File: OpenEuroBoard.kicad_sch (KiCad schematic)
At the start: 143 parts, among them J1 Eurorack_bus_mini, J10 Jack 4, J11 Conn_01x08, J12 Jack 5, J13 Jack 6, J14 Jack 7, J15 Jack 8, J16 Conn_01x04, J17 MIDI_in, J18 Conn_01x03, J19 Conn_01x03, J2 Conn_01x07, J20 Conn_01x03, J21 MIDI_out, J22 Conn_01x03, J23 Conn_01x05, J24 Conn_01x03, J25 Conn_01x05, J26 Conn_01x03, J27 Conn_01x08, J28 Conn_01x08, J29 Conn_01x04, J3 Conn_01x07, J30 Screw_Terminal_01x01, J31 Conn_01x05, J32 Conn_01x03, J33 Conn_01x05, J34 Conn_01x03, J35 Conn_01x05, J36 Conn_01x03, J37 Screw_Terminal_01x01, J38 Screw_Terminal_01x01, J39 Conn_01x05, J4 Conn_01x07, J40 Conn_01x03, J41 Conn_01x03, J42 Conn_01x05, J43 Conn_01x03, J44 Conn_01x03, J45 Conn_01x02, J46 Conn_01x04, J47 Screw_Terminal_01x01, J48 Screw_Terminal_01x01, J49 Screw_Terminal_01x01, J5 Conn_01x07, J50 Screw_Terminal_01x01, J51 Screw_Terminal_01x01, J52 Conn_01x04, J53 Conn_01x04, J54 Conn_01x04, J55 Jumpers, J56 Conn_01x04, J57 Conn_01x08, J58 Conn_01x02, J59 AudioJack3_Ground, J6 Jack 1, J7 Jack 2, J8 Conn_01x08, J9 Jack 3, SW1 SW_Push, SW10 SW_SPDT, SW11 SW_SPDT, SW12 SW_SPDT, SW2 SW_Push, SW3 SW_Push, SW4 SW_Push, SW5 SW_Push, SW6 SW_Push, SW7 SW_SPDT, SW8 SW_SPDT, SW9 SW_SPDT, U1 LM1117IMP-5, U2 TL074, U3 TL074, U4 CD40107BE, U5 6N139, U6 TL074, U7 TL072, U8 TL074

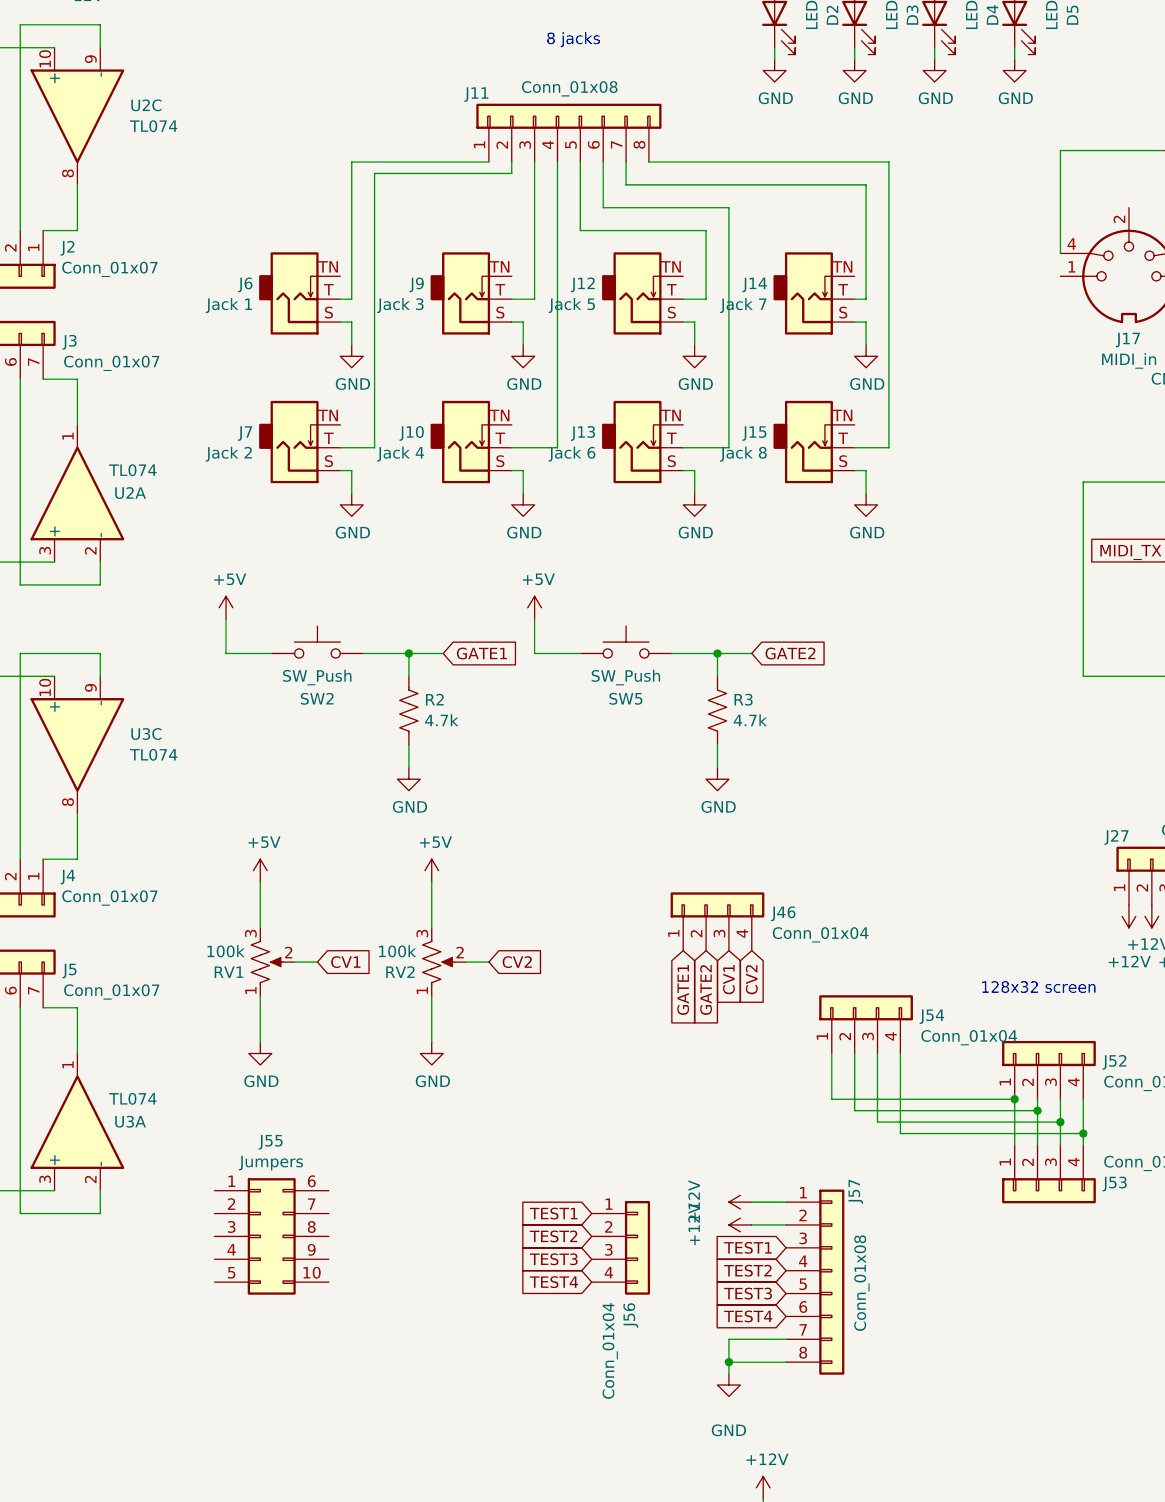
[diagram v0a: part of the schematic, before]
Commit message: Add connector for normals to jacks
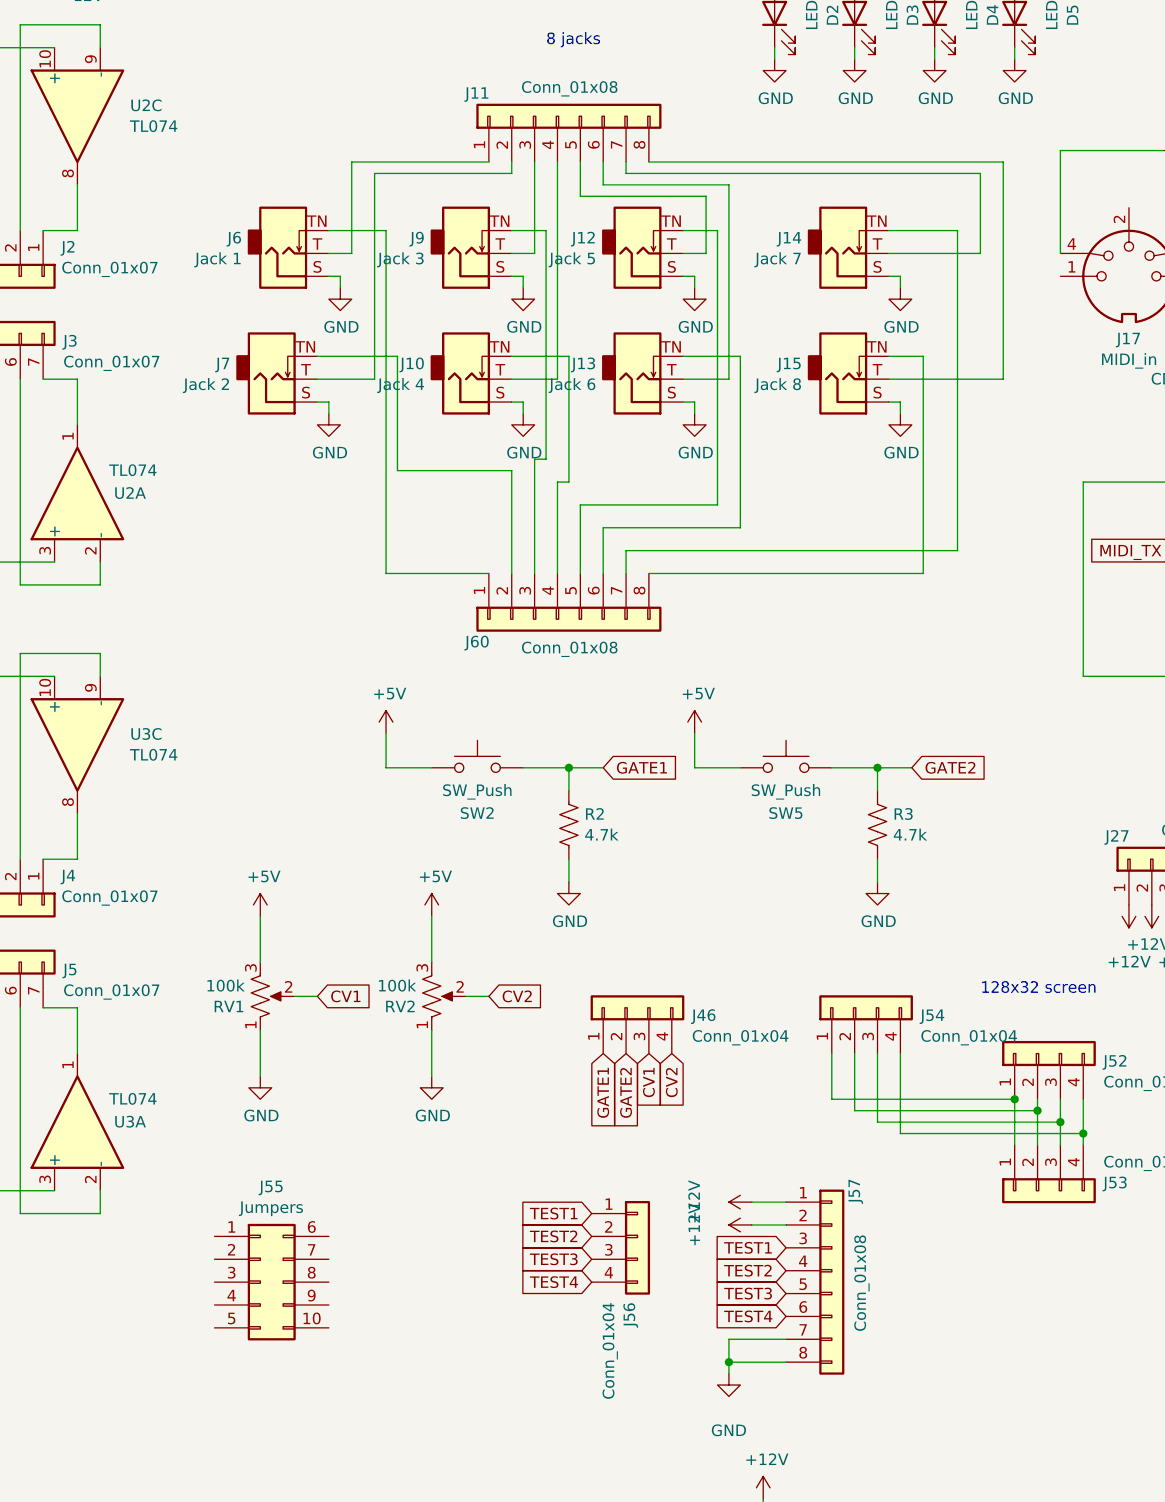
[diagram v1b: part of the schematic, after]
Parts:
- added J60: Conn_01x08, Connector_PinHeader_2.54mm:PinHeader_1x08_P2.54mm_Vertical, symbol Connector_Generic:Conn_01x08
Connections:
- net at J6.TN: now also J60.1 (Pin_1)
- net at J9.TN: now also J60.3 (Pin_3)
- net at J12.TN: now also J60.5 (Pin_5)
- net at J14.TN: now also J60.7 (Pin_7)
- net at J7.TN: now also J60.2 (Pin_2)
- net at J10.TN: now also J60.4 (Pin_4)
- net at J13.TN: now also J60.6 (Pin_6)
- net at J15.TN: now also J60.8 (Pin_8)
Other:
- moved on the sheet: J10, J12, J13, J14, J15, J46, J55, J6, J7, J9, R2, R3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
